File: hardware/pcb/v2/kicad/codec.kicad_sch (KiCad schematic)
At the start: 22 parts, among them U1 TLV320AIC3104IRHBR, U2 XC6206P182MR

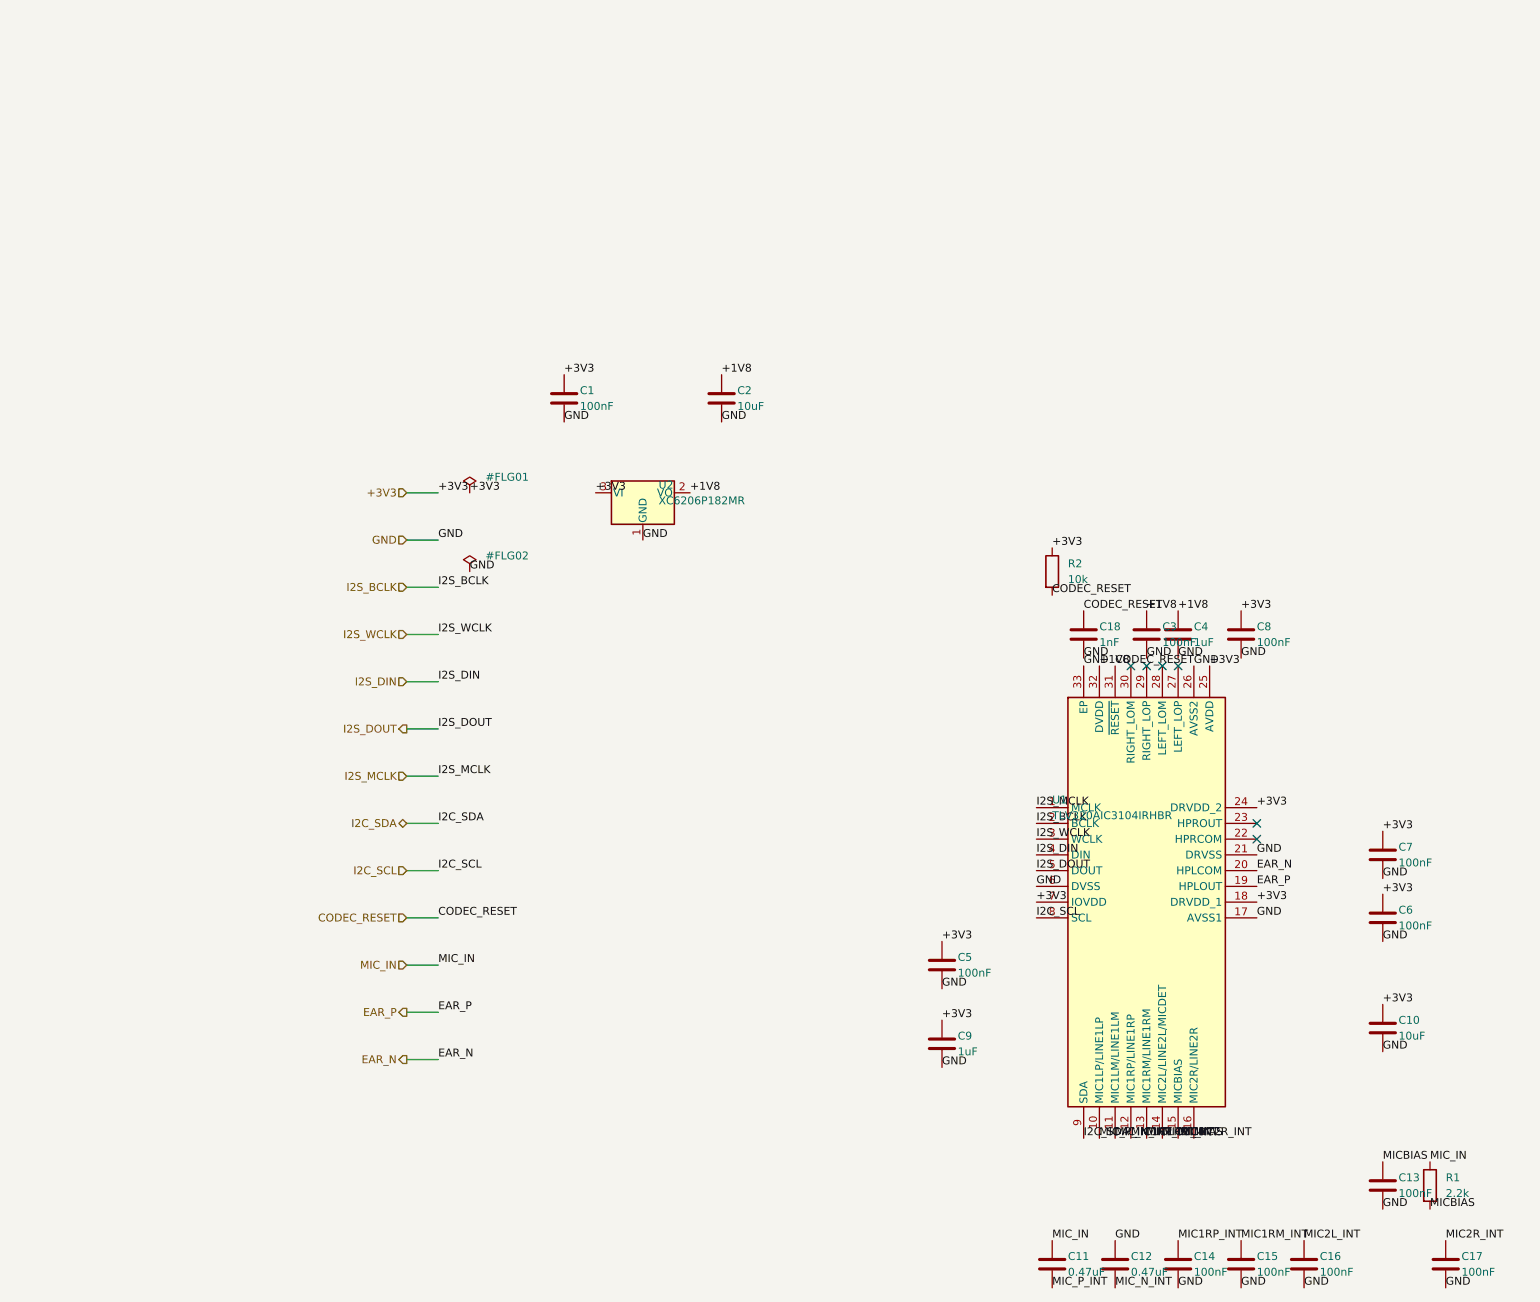
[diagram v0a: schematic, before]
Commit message: fix(hardware): rename codec sheet ports to match parent net naming
Investigation of the parent digits-pcb.kicad_sch via kicad-cli netlist
export shows the parent already uses CODEC_BCLK / CODEC_WCLK / CODEC_DIN /
CODEC_DOUT / CODEC_MCLK / CODEC_SDA / CODEC_SCL / CODEC_RESET for its Pi
header I2S/I2C connections, plus MIC_FROM_SW (post-mic-kill-switch) and
EAR_P / EAR_N for the handset audio. My initial codec module spec used
I2S_* and I2C_* port names, which would have required an extra layer of
label-to-label adapters at Phase 3 integration time.

Rename the 8 sheet ports so they match the parent net names verbatim:

  I2S_BCLK  -> CODEC_BCLK
  I2S_WCLK  -> CODEC_WCLK
  I2S_DIN   -> CODEC_DIN
  I2S_DOUT  -> CODEC_DOUT
  I2S_MCLK  -> CODEC_MCLK
  I2C_SDA   -> CODEC_SDA
  I2C_SCL   -> CODEC_SCL
  MIC_IN    -> MIC_FROM_SW

Phase 3 integration now becomes: instantiate the sheet, draw wires from
each sheet pin to the nearest existing parent net. No label-rename layer.

codec-module-spec.md §3 table and §10 updated to document the resolved
parent-net matching. check_codec_subsheet.py's EXPECTED_PORTS updated.
All 19 invariants still PASS.
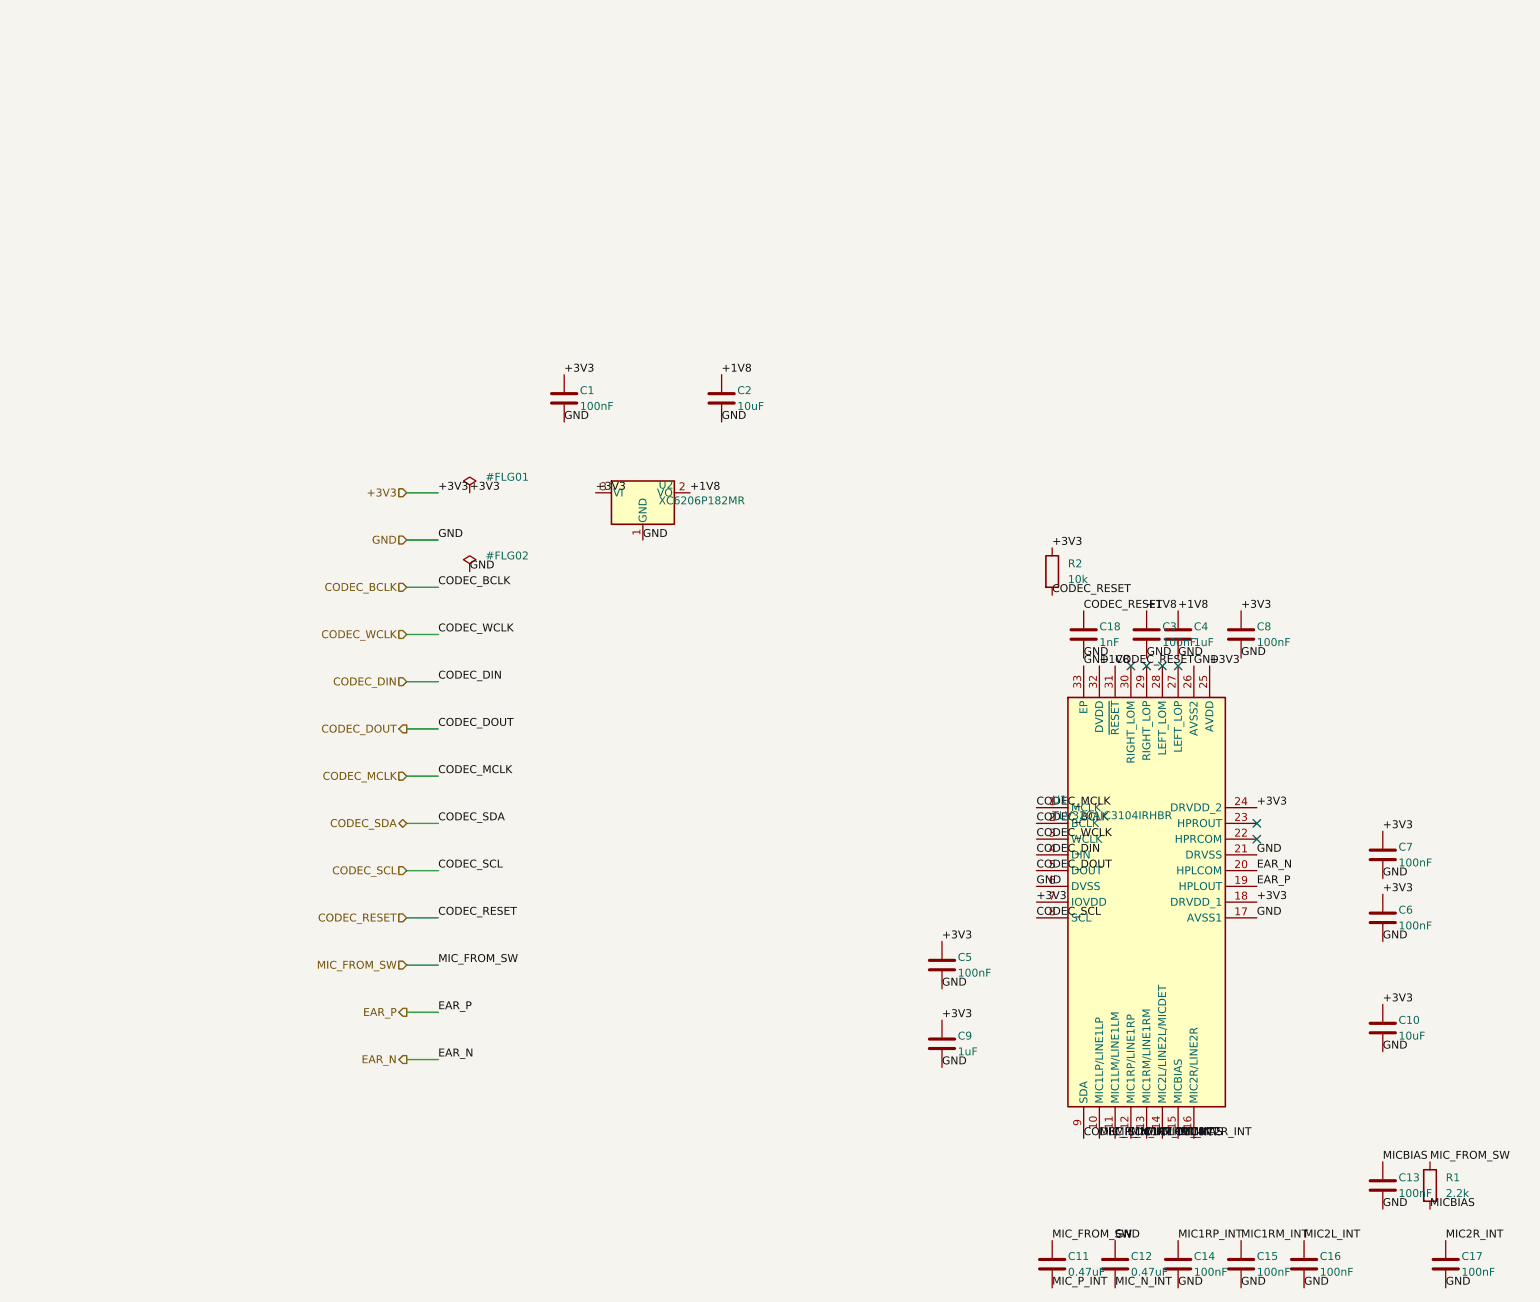
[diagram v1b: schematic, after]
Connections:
- net I2C_SCL renamed CODEC_SCL
- net I2C_SDA renamed CODEC_SDA
- net I2S_BCLK renamed CODEC_BCLK
- net I2S_DIN renamed CODEC_DIN
- net I2S_DOUT renamed CODEC_DOUT
- net I2S_MCLK renamed CODEC_MCLK
- net I2S_WCLK renamed CODEC_WCLK
- net MIC_IN renamed MIC_FROM_SW
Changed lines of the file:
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@@
   (label "+3V3" (at 208.28 158.75 0) (effects (font (size 1.27 1.27)) (justify left bottom)))
   (label "GND" (at 208.28 166.37 0) (effects (font (size 1.27 1.27)) (justify left bottom)))
-  (label "MIC_IN" (at 154.94 196.85 0) (effects (font (size 1.27 1.27)) (justify left bottom)))
+  (label "MIC_FROM_SW" (at 154.94 196.85 0) (effects (font (size 1.27 1.27)) (justify left bottom)))
   (label "MIC_P_INT" (at 154.94 204.47 0) (effects (font (size 1.27 1.27)) (justify left bottom)))
   (label "GND" (at 165.1 196.85 0) (effects (font (size 1.27 1.27)) (justify left bottom)))
@@
   (label "CODEC_RESET" (at 160.02 95.25 0) (effects (font (size 1.27 1.27)) (justify left bottom)))
   (label "GND" (at 160.02 102.87 0) (effects (font (size 1.27 1.27)) (justify left bottom)))
-  (label "MIC_IN" (at 215.9 184.15 0) (effects (font (size 1.27 1.27)) (justify left bottom)))
+  (label "MIC_FROM_SW" (at 215.9 184.15 0) (effects (font (size 1.27 1.27)) (justify left bottom)))
   (label "MICBIAS" (at 215.9 191.77 0) (effects (font (size 1.27 1.27)) (justify left bottom)))
   (label "+3V3" (at 154.94 85.09 0) (effects (font (size 1.27 1.27)) (justify left bottom)))
   (label "CODEC_RESET" (at 154.94 92.71000000000001 0) (effects (font (size 1.27 1.27)) (justify left bottom)))
-  (label "I2S_MCLK" (at 152.4 127.0 0) (effects (font (size 1.27 1.27)) (justify left bottom)))
-  (label "I2S_BCLK" (at 152.4 129.54 0) (effects (font (size 1.27 1.27)) (justify left bottom)))
-  (label "I2S_WCLK" (at 152.4 132.08 0) (effects (font (size 1.27 1.27)) (justify left bottom)))
-  (label "I2S_DIN" (at 152.4 134.62 0) (effects (font (size 1.27 1.27)) (justify left bottom)))
-  (label "I2S_DOUT" (at 152.4 137.16 0) (effects (font (size 1.27 1.27)) (justify left bottom)))
+  (label "CODEC_MCLK" (at 152.4 127.0 0) (effects (font (size 1.27 1.27)) (justify left bottom)))
+  (label "CODEC_BCLK" (at 152.4 129.54 0) (effects (font (size 1.27 1.27)) (justify left bottom)))
+  (label "CODEC_WCLK" (at 152.4 132.08 0) (effects (font (size 1.27 1.27)) (justify left bottom)))
+  (label "CODEC_DIN" (at 152.4 134.62 0) (effects (font (size 1.27 1.27)) (justify left bottom)))
+  (label "CODEC_DOUT" (at 152.4 137.16 0) (effects (font (size 1.27 1.27)) (justify left bottom)))
   (label "GND" (at 152.4 139.7 0) (effects (font (size 1.27 1.27)) (justify left bottom)))
   (label "+3V3" (at 152.4 142.24 0) (effects (font (size 1.27 1.27)) (justify left bottom)))
-  (label "I2C_SCL" (at 152.4 144.78 0) (effects (font (size 1.27 1.27)) (justify left bottom)))
-  (label "I2C_SDA" (at 160.02 180.34 0) (effects (font (size 1.27 1.27)) (justify left bottom)))
+  (label "CODEC_SCL" (at 152.4 144.78 0) (effects (font (size 1.27 1.27)) (justify left bottom)))
+  (label "CODEC_SDA" (at 160.02 180.34 0) (effects (font (size 1.27 1.27)) (justify left bottom)))
   (label "MIC_P_INT" (at 162.56 180.34 0) (effects (font (size 1.27 1.27)) (justify left bottom)))
   (label "MIC_N_INT" (at 165.1 180.34 0) (effects (font (size 1.27 1.27)) (justify left bottom)))
@@
   (label "+3V3" (at 55.879999999999995 76.2 0) (effects (font (size 1.27 1.27)) (justify left bottom)))
   (label "GND" (at 55.879999999999995 83.82000000000001 0) (effects (font (size 1.27 1.27)) (justify left bottom)))
-  (label "I2S_BCLK" (at 55.879999999999995 91.44000000000001 0) (effects (font (size 1.27 1.27)) (justify left bottom)))
-  (label "I2S_WCLK" (at 55.879999999999995 99.06000000000002 0) (effects (font (size 1.27 1.27)) (justify left bottom)))
-  (label "I2S_DIN" (at 55.879999999999995 106.68000000000002 0) (effects (font (size 1.27 1.27)) (justify left bottom)))
-  (label "I2S_DOUT" (at 55.879999999999995 114.30000000000003 0) (effects (font (size 1.27 1.27)) (justify left bottom)))
-  (label "I2S_MCLK" (at 55.879999999999995 121.92000000000003 0) (effects (font (size 1.27 1.27)) (justify left bottom)))
-  (label "I2C_SDA" (at 55.879999999999995 129.54000000000002 0) (effects (font (size 1.27 1.27)) (justify left bottom)))
-  (label "I2C_SCL" (at 55.879999999999995 137.16000000000003 0) (effects (font (size 1.27 1.27)) (justify left bottom)))
+  (label "CODEC_BCLK" (at 55.879999999999995 91.44000000000001 0) (effects (font (size 1.27 1.27)) (justify left bottom)))
+  (label "CODEC_WCLK" (at 55.879999999999995 99.06000000000002 0) (effects (font (size 1.27 1.27)) (justify left bottom)))
+  (label "CODEC_DIN" (at 55.879999999999995 106.68000000000002 0) (effects (font (size 1.27 1.27)) (justify left bottom)))
+  (label "CODEC_DOUT" (at 55.879999999999995 114.30000000000003 0) (effects (font (size 1.27 1.27)) (justify left bottom)))
+  (label "CODEC_MCLK" (at 55.879999999999995 121.92000000000003 0) (effects (font (size 1.27 1.27)) (justify left bottom)))
+  (label "CODEC_SDA" (at 55.879999999999995 129.54000000000002 0) (effects (font (size 1.27 1.27)) (justify left bottom)))
+  (label "CODEC_SCL" (at 55.879999999999995 137.16000000000003 0) (effects (font (size 1.27 1.27)) (justify left bottom)))
   (label "CODEC_RESET" (at 55.879999999999995 144.78000000000003 0) (effects (font (size 1.27 1.27)) (justify left bottom)))
-  (label "MIC_IN" (at 55.879999999999995 152.40000000000003 0) (effects (font (size 1.27 1.27)) (justify left bottom)))
+  (label "MIC_FROM_SW" (at 55.879999999999995 152.40000000000003 0) (effects (font (size 1.27 1.27)) (justify left bottom)))
   (label "EAR_P" (at 55.879999999999995 160.02000000000004 0) (effects (font (size 1.27 1.27)) (justify left bottom)))
   (label "EAR_N" (at 55.879999999999995 167.64000000000004 0) (effects (font (size 1.27 1.27)) (justify left bottom)))
   (hierarchical_label "+3V3" (shape input) (at 50.8 76.2 180) (effects (font (size 1.27 1.27)) (justify right)))
   (hierarchical_label "GND" (shape input) (at 50.8 83.82000000000001 180) (effects (font (size 1.27 1.27)) (justify right)))
-  (hierarchical_label "I2S_BCLK" (shape input) (at 50.8 91.44000000000001 180) (effects (font (size 1.27 1.27)) (justify right)))
-  (hierarchical_label "I2S_WCLK" (shape input) (at 50.8 99.06000000000002 180) (effects (font (size 1.27 1.27)) (justify right)))
-  (hierarchical_label "I2S_DIN" (shape input) (at 50.8 106.68000000000002 180) (effects (font (size 1.27 1.27)) (justify right)))
-  (hierarchical_label "I2S_DOUT" (shape output) (at 50.8 114.30000000000003 180) (effects (font (size 1.27 1.27)) (justify right)))
-  (hierarchical_label "I2S_MCLK" (shape input) (at 50.8 121.92000000000003 180) (effects (font (size 1.27 1.27)) (justify right)))
-  (hierarchical_label "I2C_SDA" (shape bidirectional) (at 50.8 129.54000000000002 180) (effects (font (size 1.27 1.27)) (justify right)))
-  (hierarchical_label "I2C_SCL" (shape input) (at 50.8 137.16000000000003 180) (effects (font (size 1.27 1.27)) (justify right)))
+  (hierarchical_label "CODEC_BCLK" (shape input) (at 50.8 91.44000000000001 180) (effects (font (size 1.27 1.27)) (justify right)))
+  (hierarchical_label "CODEC_WCLK" (shape input) (at 50.8 99.06000000000002 180) (effects (font (size 1.27 1.27)) (justify right)))
+  (hierarchical_label "CODEC_DIN" (shape input) (at 50.8 106.68000000000002 180) (effects (font (size 1.27 1.27)) (justify right)))
+  (hierarchical_label "CODEC_DOUT" (shape output) (at 50.8 114.30000000000003 180) (effects (font (size 1.27 1.27)) (justify right)))
+  (hierarchical_label "CODEC_MCLK" (shape input) (at 50.8 121.92000000000003 180) (effects (font (size 1.27 1.27)) (justify right)))
+  (hierarchical_label "CODEC_SDA" (shape bidirectional) (at 50.8 129.54000000000002 180) (effects (font (size 1.27 1.27)) (justify right)))
+  (hierarchical_label "CODEC_SCL" (shape input) (at 50.8 137.16000000000003 180) (effects (font (size 1.27 1.27)) (justify right)))
   (hierarchical_label "CODEC_RESET" (shape input) (at 50.8 144.78000000000003 180) (effects (font (size 1.27 1.27)) (justify right)))
-  (hierarchical_label "MIC_IN" (shape input) (at 50.8 152.40000000000003 180) (effects (font (size 1.27 1.27)) (justify right)))
+  (hierarchical_label "MIC_FROM_SW" (shape input) (at 50.8 152.40000000000003 180) (effects (font (size 1.27 1.27)) (justify right)))
   (hierarchical_label "EAR_P" (shape output) (at 50.8 160.02000000000004 180) (effects (font (size 1.27 1.27)) (justify right)))
   (hierarchical_label "EAR_N" (shape output) (at 50.8 167.64000000000004 180) (effects (font (size 1.27 1.27)) (justify right)))

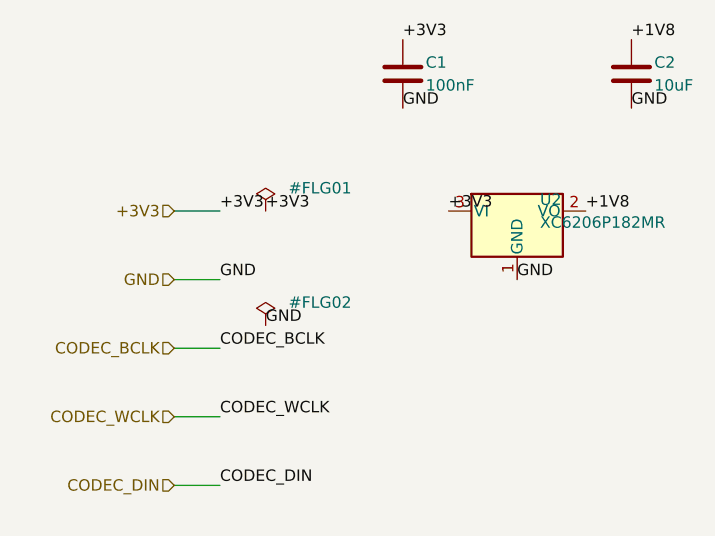
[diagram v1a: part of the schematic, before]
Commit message: feat(hardware): integrate codec.kicad_sch hierarchical sheet into main schematic
Phase 3 Task 3.2 of the compartmentalized rebuild plan. Instantiates the
self-contained codec subsheet in the main schematic and wires its 13
sheet pins to the existing global labels on J1 (Pi header), J8 (handset
RJ9), J9 (mic kill switch), and J10 (earpiece intermediate), plus two
power symbols on +3V3 and GND.

Sheet placed at (200, 180) with size (60, 100) in the area cleared by
the U6 teardown. Each sheet pin connects via a short wire to a
global_label (11 nets) or a power symbol (+3V3, GND) so the nets bridge
across sheets by name.

Refdes collisions between the codec subsheet (U1, U2, R1, R2, C1-C18)
and the main schematic were resolved by adding a second instance path
inside codec.kicad_sch that re-maps those refs under the parent project:
U1->U6, U2->U7, R1->R10, R2->R11, C1-C18->C36-C53. The standalone codec
sheet keeps its original refs so check_codec_subsheet.py still works.

Removed the two PWR_FLAG symbols from codec.kicad_sch (+3V3 and GND)
plus the two dangling local labels they left behind. They were only
there to satisfy standalone ERC and now conflict with the main U5 LDO
and the parent's existing +3V3/GND power flags.

Verification:
- kicad-cli sch erc: 0 errors, 0 warnings on the integrated schematic
- kicad-cli sch export netlist: 77 components total, no duplicate refs
- 13 codec sheet pins all bridge to their parent labels (CODEC_BCLK..
  EAR_N each >=2 nodes; +3V3 has 42 nodes; GND has 75 nodes)
- RP2040 cluster intact (U3, U4, Y1 present)
- All 4 project checkers pass: check_codec_symbol, check_codec_subsheet,
  check_decoupling, check_rp2040_bom
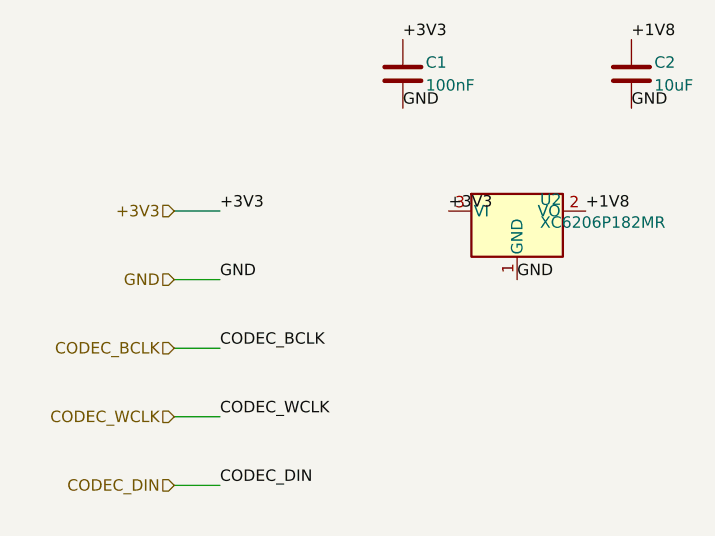
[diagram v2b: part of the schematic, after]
